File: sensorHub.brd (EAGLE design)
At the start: 70 x 70 mm, 11 parts

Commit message: Connects the sht10 pins from SDA and SCL to pin 10 and pin 12 respectively
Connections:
- removed net N$20: JP2.7, JP2.8
- removed net N$22: JP2.11, JP2.12
- new net 10_SDA: JP2.11, JP2.12, SHT10.4
- new net 12_SCL: JP2.7, JP2.8, SHT10.3
- net SCL: no longer SHT10.3
- net SDA: no longer SHT10.4
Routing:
- net SDA: track 117.2 -> 103.1 mm
- net SCL: track 120.6 -> 106.5 mm
- net N$22: track 2.54 -> 0.00 mm
- net N$20: track 2.54 -> 0.00 mm
- net 12_SCL: track 0.00 -> 2.54 mm
- net 10_SDA: track 0.00 -> 2.54 mm
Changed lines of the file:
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@@
 <wire x1="54.05" y1="45.87" x2="56.59" y2="45.87" width="1.27" layer="16"/>
-</signal>
-<signal name="N$20">
-<contactref element="JP2" pad="7"/>
-<contactref element="JP2" pad="8"/>
-<wire x1="54.05" y1="43.33" x2="56.59" y2="43.33" width="1.27" layer="16"/>
 </signal>
 <signal name="N$21">
@@
 <contactref element="JP2" pad="10"/>
 <wire x1="54.05" y1="40.79" x2="56.59" y2="40.79" width="1.27" layer="16"/>
-</signal>
-<signal name="N$22">
-<contactref element="JP2" pad="11"/>
-<contactref element="JP2" pad="12"/>
-<wire x1="54.05" y1="38.25" x2="56.59" y2="38.25" width="1.27" layer="16"/>
 </signal>
 <signal name="N$23">
@@
 <contactref element="JP2" pad="20"/>
 <contactref element="LUX" pad="3"/>
-<contactref element="SHT10" pad="3"/>
 <contactref element="R1" pad="2"/>
-<wire x1="3.49" y1="60.89" x2="17.58" y2="60.89" width="1.27" layer="16"/>
 <wire x1="17.59" y1="60.9" x2="17.62" y2="60.93" width="1.27" layer="16"/>
 <wire x1="54.05" y1="28.09" x2="56.59" y2="28.09" width="1.27" layer="16"/>
@@
 <contactref element="JP2" pad="22"/>
 <contactref element="LUX" pad="4"/>
-<contactref element="SHT10" pad="4"/>
 <contactref element="R2" pad="2"/>
-<wire x1="3.49" y1="64.39" x2="17.58" y2="64.39" width="1.27" layer="16"/>
 <wire x1="17.58" y1="64.39" x2="17.62" y2="64.43" width="1.27" layer="16"/>
 <wire x1="54.05" y1="25.55" x2="56.59" y2="25.55" width="1.27" layer="16"/>
@@
 <wire x1="15.71" y1="10.29" x2="23.6" y2="2.4" width="1.27" layer="16"/>
 </signal>
+<signal name="10_SDA">
+<contactref element="SHT10" pad="4"/>
+<contactref element="JP2" pad="11"/>
+<contactref element="JP2" pad="12"/>
+<wire x1="54.05" y1="38.25" x2="56.59" y2="38.25" width="1.27" layer="16"/>
+<wire x1="3.49" y1="64.39" x2="54.05" y2="38.25" width="0" layer="19" extent="1-1"/>
+</signal>
+<signal name="12_SCL">
+<contactref element="SHT10" pad="3"/>
+<contactref element="JP2" pad="7"/>
+<contactref element="JP2" pad="8"/>
+<wire x1="54.05" y1="43.33" x2="56.59" y2="43.33" width="1.27" layer="16"/>
+<wire x1="3.49" y1="60.89" x2="54.05" y2="43.33" width="0" layer="19" extent="1-1"/>
+</signal>
 </signals>

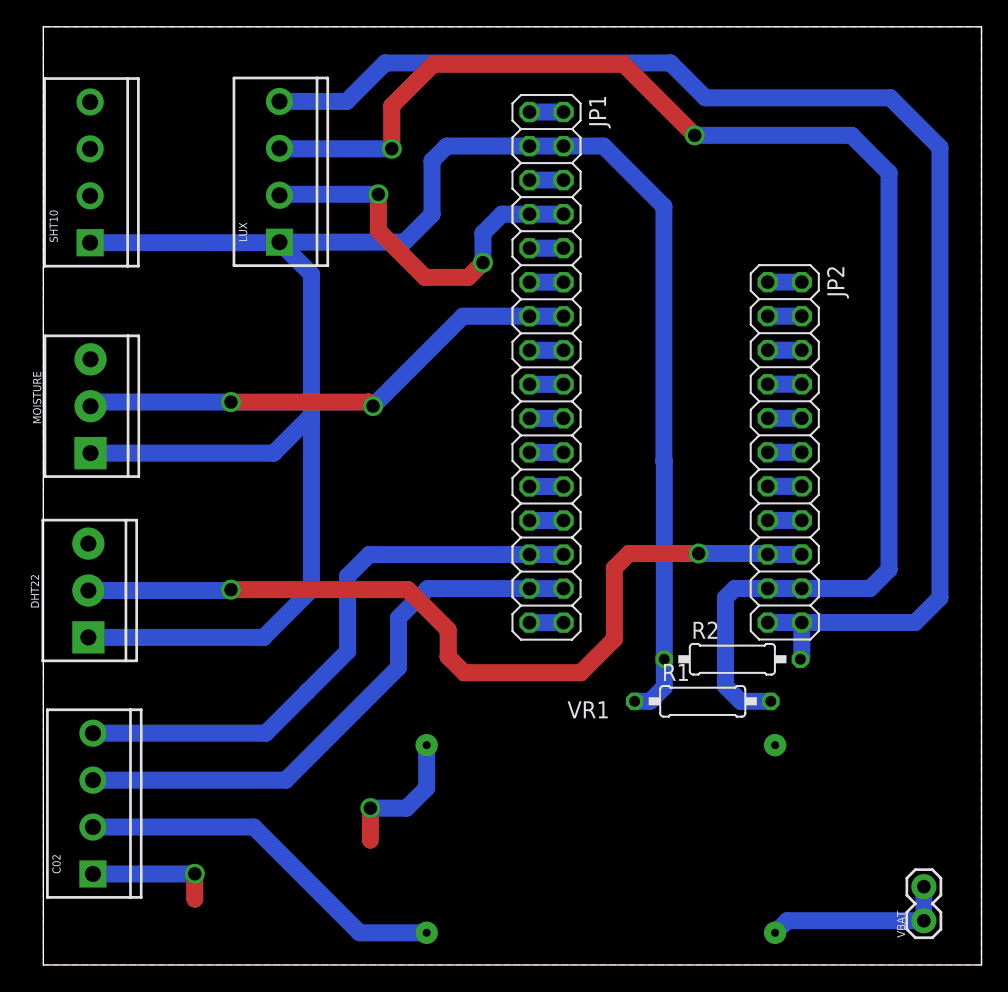
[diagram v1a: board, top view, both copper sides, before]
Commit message: Transfers the sht schematic changes to the brd file
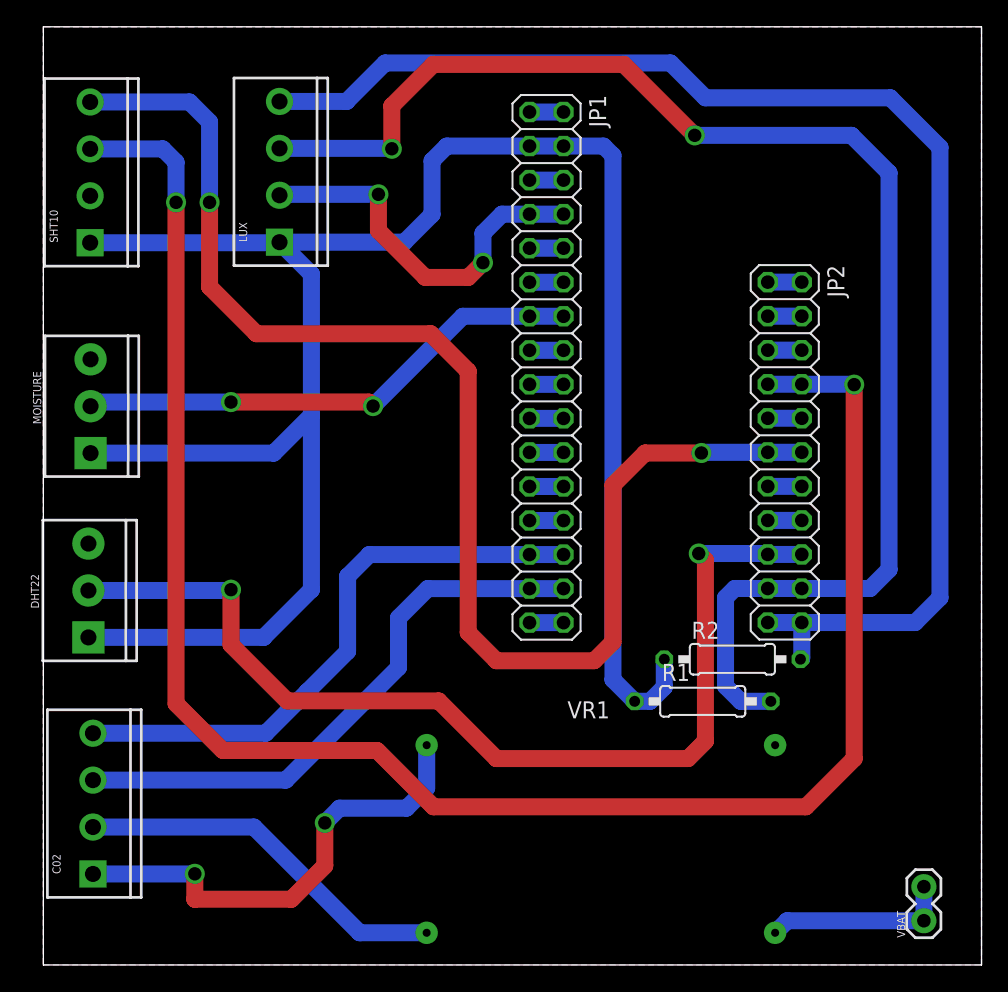
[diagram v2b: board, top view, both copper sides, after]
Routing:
- net 12_SCL: track 2.54 -> 136.9 mm, vias 0 -> 2
- net 10_SDA: track 2.54 -> 102.3 mm, vias 0 -> 2
- net GND: track 48.5 -> 63.9 mm
- net D5: track 63.8 -> 76.2 mm
- net 3V: track 151.2 -> 153.4 mm
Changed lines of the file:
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@@
 <setting verticaltext="up"/>
 </settings>
-<grid distance="1" unitdist="mm" unit="mm" style="dots" multiple="1" display="yes" altdistance="5" altunitdist="mil" altunit="mm"/>
+<grid distance="0.1" unitdist="mm" unit="mm" style="dots" multiple="1" display="yes" altdistance="5" altunitdist="mil" altunit="mm"/>
 <layers>
 <layer number="1" name="Top" color="4" fill="1" visible="yes" active="yes"/>
@@
 <wire x1="11.29" y1="6.79" x2="11.3" y2="6.8" width="1.27" layer="16"/>
 <via x="11.3" y="6.8" extent="1-16" drill="1" diameter="1"/>
-<wire x1="11.3" y1="6.8" x2="11.3" y2="4.9" width="1.27" layer="1"/>
+<wire x1="11.3" y1="4.9" x2="11.3" y2="6.8" width="1.27" layer="1"/>
 <wire x1="28.6" y1="16.4" x2="28.6" y2="13.2" width="1.27" layer="16"/>
-<wire x1="27.1" y1="11.7" x2="24.4" y2="11.7" width="1.27" layer="16"/>
-<via x="24.4" y="11.7" extent="1-16" drill="1" diameter="1"/>
-<wire x1="24.4" y1="11.7" x2="24.4" y2="9.3" width="1.27" layer="1"/>
 <wire x1="28.6" y1="13.2" x2="27.1" y2="11.7" width="1.27" layer="16"/>
 <wire x1="36.273" y1="56.021" x2="34.221" y2="56.021" width="1.27" layer="16"/>
@@
 <vertex x="0" y="70"/>
 </polygon>
+<wire x1="22.1" y1="11.7" x2="21" y2="10.6" width="1.27" layer="16"/>
+<via x="21" y="10.6" extent="1-16" drill="1" diameter="1.3"/>
+<wire x1="21" y1="10.6" x2="21" y2="7.4" width="1.27" layer="1"/>
+<wire x1="18.5" y1="4.9" x2="11.3" y2="4.9" width="1.27" layer="1"/>
+<wire x1="27.1" y1="11.7" x2="22.1" y2="11.7" width="1.27" layer="16"/>
+<wire x1="21" y1="7.4" x2="18.5" y2="4.9" width="1.27" layer="1"/>
 </signal>
 <signal name="N$1">
@@
 <wire x1="36.273" y1="61.101" x2="38.813" y2="61.101" width="1.27" layer="16"/>
 <wire x1="38.813" y1="61.101" x2="41.799" y2="61.101" width="1.27" layer="16"/>
-<wire x1="46.3" y1="37.6" x2="46.3" y2="56.6" width="1.27" layer="16"/>
-<wire x1="41.799" y1="61.101" x2="46.3" y2="56.6" width="1.27" layer="16"/>
-<wire x1="46.33" y1="22.81" x2="46.33" y2="37.57" width="1.27" layer="16"/>
-<wire x1="46.33" y1="37.57" x2="46.3" y2="37.6" width="1.27" layer="16"/>
 <wire x1="46.33" y1="22.81" x2="46.33" y2="20.73" width="1.27" layer="16"/>
 <wire x1="45.27" y1="19.67" x2="44.12" y2="19.67" width="1.27" layer="16"/>
 <wire x1="46.33" y1="20.73" x2="45.27" y2="19.67" width="1.27" layer="16"/>
+<wire x1="44.12" y1="19.67" x2="42.5" y2="21.29" width="1.27" layer="16"/>
+<wire x1="42.5" y1="60.4" x2="41.799" y2="61.101" width="1.27" layer="16"/>
+<wire x1="42.5" y1="21.29" x2="42.5" y2="60.4" width="1.27" layer="16"/>
 </signal>
 <signal name="N$3">
@@
 <wire x1="13.94" y1="27.94" x2="14" y2="28" width="1.27" layer="16"/>
 <via x="14" y="28" extent="1-16" drill="1" diameter="1"/>
-<wire x1="30.2" y1="25" x2="30.2" y2="23" width="1.27" layer="1"/>
-<wire x1="14" y1="28" x2="27.2" y2="28" width="1.27" layer="1"/>
-<wire x1="27.2" y1="28" x2="30.2" y2="25" width="1.27" layer="1"/>
-<wire x1="30.2" y1="23" x2="31.4" y2="21.8" width="1.27" layer="1"/>
-<wire x1="42.6" y1="24.3" x2="42.6" y2="29.6" width="1.27" layer="1"/>
-<wire x1="42.6" y1="29.6" x2="43.7" y2="30.7" width="1.27" layer="1"/>
-<wire x1="43.7" y1="30.7" x2="48.9" y2="30.7" width="1.27" layer="1"/>
 <via x="48.9" y="30.7" extent="1-16" drill="1" diameter="1"/>
 <wire x1="48.9" y1="30.7" x2="53.98" y2="30.7" width="1.27" layer="16"/>
 <wire x1="53.98" y1="30.7" x2="54.05" y2="30.63" width="1.27" layer="16"/>
-<wire x1="31.4" y1="21.8" x2="40.1" y2="21.8" width="1.27" layer="1"/>
-<wire x1="40.1" y1="21.8" x2="42.6" y2="24.3" width="1.27" layer="1"/>
+<wire x1="14" y1="28" x2="14" y2="23.9" width="1.27" layer="1"/>
+<wire x1="49.4" y1="16.7" x2="48.1" y2="15.4" width="1.27" layer="1"/>
+<wire x1="49.4" y1="16.7" x2="49.4" y2="30.2" width="1.27" layer="1"/>
+<wire x1="49.4" y1="30.2" x2="48.9" y2="30.7" width="1.27" layer="1"/>
+<wire x1="18.2" y1="19.7" x2="14" y2="23.9" width="1.27" layer="1"/>
+<wire x1="29.5" y1="19.7" x2="18.2" y2="19.7" width="1.27" layer="1"/>
+<wire x1="48.1" y1="15.4" x2="33.8" y2="15.4" width="1.27" layer="1"/>
+<wire x1="33.8" y1="15.4" x2="29.5" y2="19.7" width="1.27" layer="1"/>
 </signal>
 <signal name="SCL">
@@
 <contactref element="LUX" pad="3"/>
 <contactref element="R1" pad="2"/>
-<wire x1="17.59" y1="60.9" x2="17.62" y2="60.93" width="1.27" layer="16"/>
 <wire x1="54.05" y1="28.09" x2="56.59" y2="28.09" width="1.27" layer="16"/>
 <wire x1="56.59" y1="28.09" x2="61.69" y2="28.09" width="1.27" layer="16"/>
@@
 <wire x1="26" y1="64.1" x2="26" y2="60.9" width="1.27" layer="1"/>
 <via x="26" y="60.9" extent="1-16" drill="1" diameter="1"/>
-<wire x1="26" y1="60.9" x2="17.59" y2="60.9" width="1.27" layer="16"/>
-<wire x1="17.59" y1="60.9" x2="17.58" y2="60.89" width="1.27" layer="16"/>
 <wire x1="63.1" y1="59.1" x2="60.3" y2="61.9" width="1.27" layer="16"/>
 <wire x1="54.05" y1="28.09" x2="51.59" y2="28.09" width="1.27" layer="16"/>
@@
 <wire x1="54.28" y1="19.67" x2="52.03" y2="19.67" width="1.27" layer="16"/>
 <wire x1="52.03" y1="19.67" x2="50.9" y2="20.8" width="1.27" layer="16"/>
+<wire x1="17.62" y1="60.93" x2="25.97" y2="60.93" width="1.27" layer="16"/>
+<wire x1="25.97" y1="60.93" x2="26" y2="60.9" width="1.27" layer="16"/>
 </signal>
 <signal name="SDA">
@@
 <contactref element="LUX" pad="4"/>
 <contactref element="R2" pad="2"/>
-<wire x1="17.58" y1="64.39" x2="17.62" y2="64.43" width="1.27" layer="16"/>
 <wire x1="54.05" y1="25.55" x2="56.59" y2="25.55" width="1.27" layer="16"/>
 <wire x1="17.62" y1="64.43" x2="22.63" y2="64.43" width="1.27" layer="16"/>
@@
 <contactref element="JP2" pad="12"/>
 <wire x1="54.05" y1="38.25" x2="56.59" y2="38.25" width="1.27" layer="16"/>
-<wire x1="3.49" y1="64.39" x2="54.05" y2="38.25" width="0" layer="19" extent="1-1"/>
+<wire x1="3.49" y1="64.39" x2="10.91" y2="64.39" width="1.27" layer="16"/>
+<wire x1="12.4" y1="62.9" x2="12.4" y2="56.9" width="1.27" layer="16"/>
+<via x="12.4" y="56.9" extent="1-16" drill="1" diameter="1.3"/>
+<wire x1="12.4" y1="50.6" x2="12.4" y2="56.9" width="1.27" layer="1"/>
+<wire x1="10.91" y1="64.39" x2="12.4" y2="62.9" width="1.27" layer="16"/>
+<wire x1="54.05" y1="38.25" x2="49.15" y2="38.25" width="1.27" layer="16"/>
+<wire x1="49.15" y1="38.25" x2="49.1" y2="38.2" width="1.27" layer="16"/>
+<via x="49.1" y="38.2" extent="1-16" drill="1" diameter="1.3"/>
+<wire x1="49.1" y1="38.2" x2="44.9" y2="38.2" width="1.27" layer="1"/>
+<wire x1="42.5" y1="35.8" x2="42.5" y2="24.1" width="1.27" layer="1"/>
+<wire x1="42.5" y1="24.1" x2="41.1" y2="22.7" width="1.27" layer="1"/>
+<wire x1="31.7" y1="24.8" x2="31.7" y2="44.3" width="1.27" layer="1"/>
+<wire x1="31.7" y1="44.3" x2="28.9" y2="47.1" width="1.27" layer="1"/>
+<wire x1="44.9" y1="38.2" x2="42.5" y2="35.8" width="1.27" layer="1"/>
+<wire x1="41.1" y1="22.7" x2="33.8" y2="22.7" width="1.27" layer="1"/>
+<wire x1="33.8" y1="22.7" x2="31.7" y2="24.8" width="1.27" layer="1"/>
+<wire x1="28.9" y1="47.1" x2="15.9" y2="47.1" width="1.27" layer="1"/>
+<wire x1="15.9" y1="47.1" x2="12.4" y2="50.6" width="1.27" layer="1"/>
 </signal>
 <signal name="12_SCL">
@@
 <contactref element="JP2" pad="8"/>
 <wire x1="54.05" y1="43.33" x2="56.59" y2="43.33" width="1.27" layer="16"/>
-<wire x1="3.49" y1="60.89" x2="54.05" y2="43.33" width="0" layer="19" extent="1-1"/>
+<wire x1="56.59" y1="43.33" x2="60.47" y2="43.33" width="1.27" layer="16"/>
+<wire x1="60.47" y1="43.33" x2="60.5" y2="43.3" width="1.27" layer="16"/>
+<via x="60.5" y="43.3" extent="1-16" drill="1" diameter="1.3"/>
+<wire x1="3.49" y1="60.89" x2="8.91" y2="60.89" width="1.27" layer="16"/>
+<wire x1="9.9" y1="59.9" x2="9.9" y2="56.9" width="1.27" layer="16"/>
+<via x="9.9" y="56.9" extent="1-16" drill="1" diameter="1.3"/>
+<wire x1="9.9" y1="56.9" x2="9.9" y2="19.5" width="1.27" layer="1"/>
+<wire x1="24.9" y1="16" x2="29.1" y2="11.8" width="1.27" layer="1"/>
+<wire x1="29.1" y1="11.8" x2="56.9" y2="11.8" width="1.27" layer="1"/>
+<wire x1="60.5" y1="15.4" x2="60.5" y2="43.3" width="1.27" layer="1"/>
+<wire x1="8.91" y1="60.89" x2="9.9" y2="59.9" width="1.27" layer="16"/>
+<wire x1="9.9" y1="19.5" x2="13.4" y2="16" width="1.27" layer="1"/>
+<wire x1="13.4" y1="16" x2="24.9" y2="16" width="1.27" layer="1"/>
+<wire x1="56.9" y1="11.8" x2="60.5" y2="15.4" width="1.27" layer="1"/>
 </signal>
 </signals>

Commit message: Reroutes the connection between the double female header pins
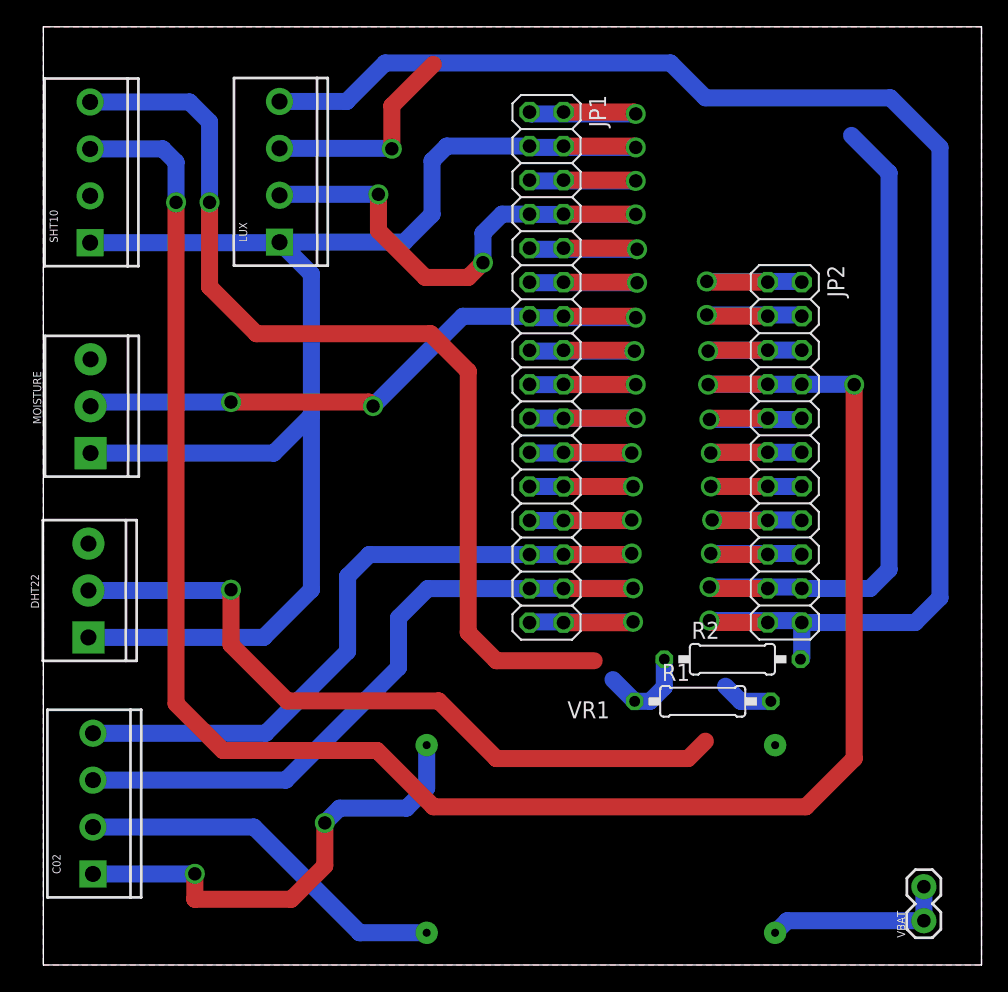
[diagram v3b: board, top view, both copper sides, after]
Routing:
- net SCL: track 106.4 -> 71.8 mm
- net 3V: track 153.4 -> 121.2 mm, vias 0 -> 1
- net 10_SDA: track 102.3 -> 84.6 mm
- net N$5: track 2.54 -> 13.6 mm, vias 0 -> 1
- net N$6: track 2.54 -> 13.5 mm, vias 0 -> 1
- net N$1: track 2.54 -> 13.4 mm, vias 0 -> 1
- net A2: track 38.3 -> 49.2 mm, vias 2 -> 3
- net D5: track 76.2 -> 65.3 mm
- net N$3: track 2.54 -> 13.4 mm, vias 0 -> 1
- net GND: track 63.9 -> 74.7 mm, vias 4 -> 5
- net N$9: track 2.54 -> 13.3 mm, vias 0 -> 1
- net N$10: track 2.54 -> 13.3 mm, vias 0 -> 1
- net N$8: track 2.54 -> 13.2 mm, vias 0 -> 1
- net N$16: track 2.54 -> 13.0 mm, vias 0 -> 1
- net TX: track 43.2 -> 53.6 mm, vias 0 -> 1
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
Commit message: Completes the rerouting of the sensor hub board
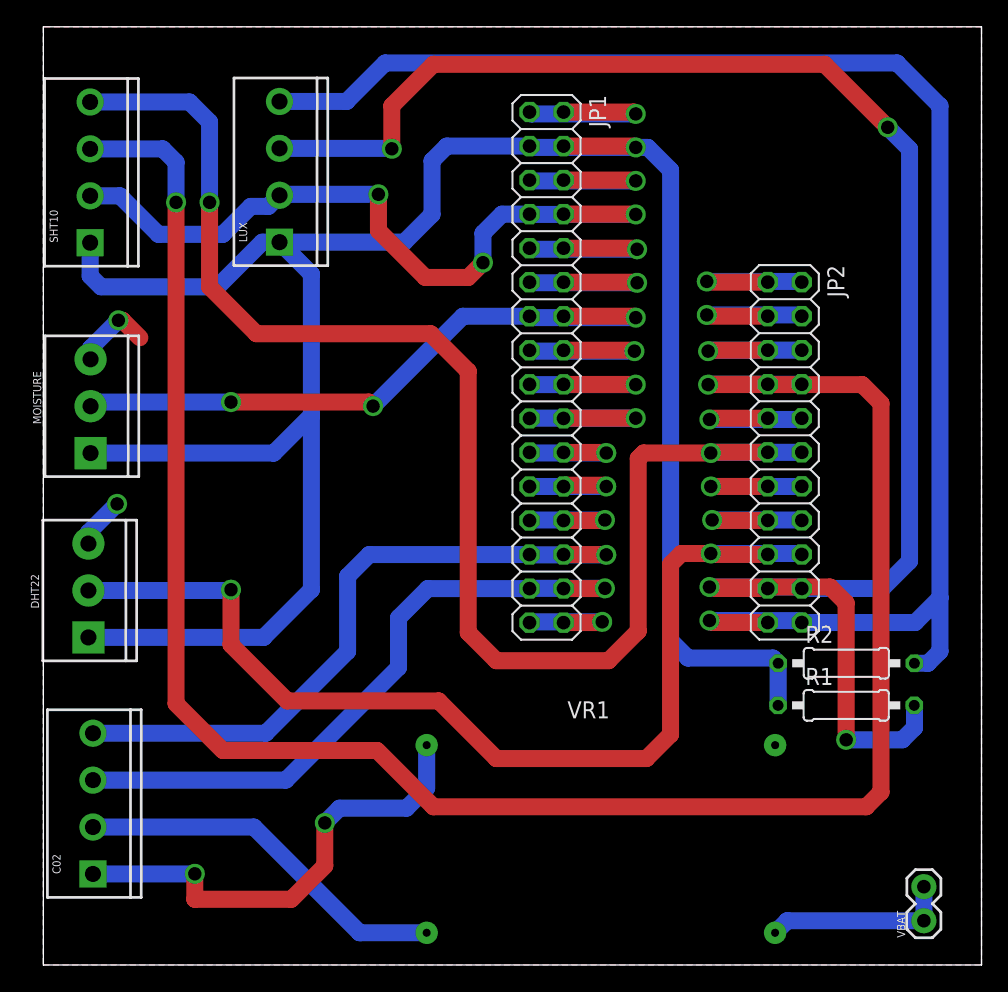
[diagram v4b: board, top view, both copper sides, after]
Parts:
- moved R1 10.7 mm to (59.9, 19.4)
- moved R2 8.51 mm to (59.9, 22.5)
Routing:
- net SCL: track 71.8 -> 133.1 mm, vias 2 -> 4
- net 3V: track 121.2 -> 168.6 mm
- net GND: track 74.7 -> 101.0 mm, vias 5 -> 7
- net 10_SDA: track 84.6 -> 107.3 mm
- net D5: track 65.3 -> 79.0 mm
- net 12_SCL: track 145.8 -> 157.4 mm, vias 3 -> 2
- net SDA: track 111.9 -> 117.2 mm
- net N$16: track 13.0 -> 8.36 mm
- net TX: track 53.6 -> 49.4 mm
- net N$13: track 12.7 -> 8.75 mm
- net N$12: track 12.9 -> 9.00 mm
- net RX: track 54.2 -> 50.3 mm
- net N$11: track 12.7 -> 8.95 mm
